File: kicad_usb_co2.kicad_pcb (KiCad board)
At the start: 2 copper layers, 90 x 54 mm, 10 parts, among them SW1 SW_Push, SW2 SW_Push, U1 MH-Z14A, U2 SeeeduinoXIAO

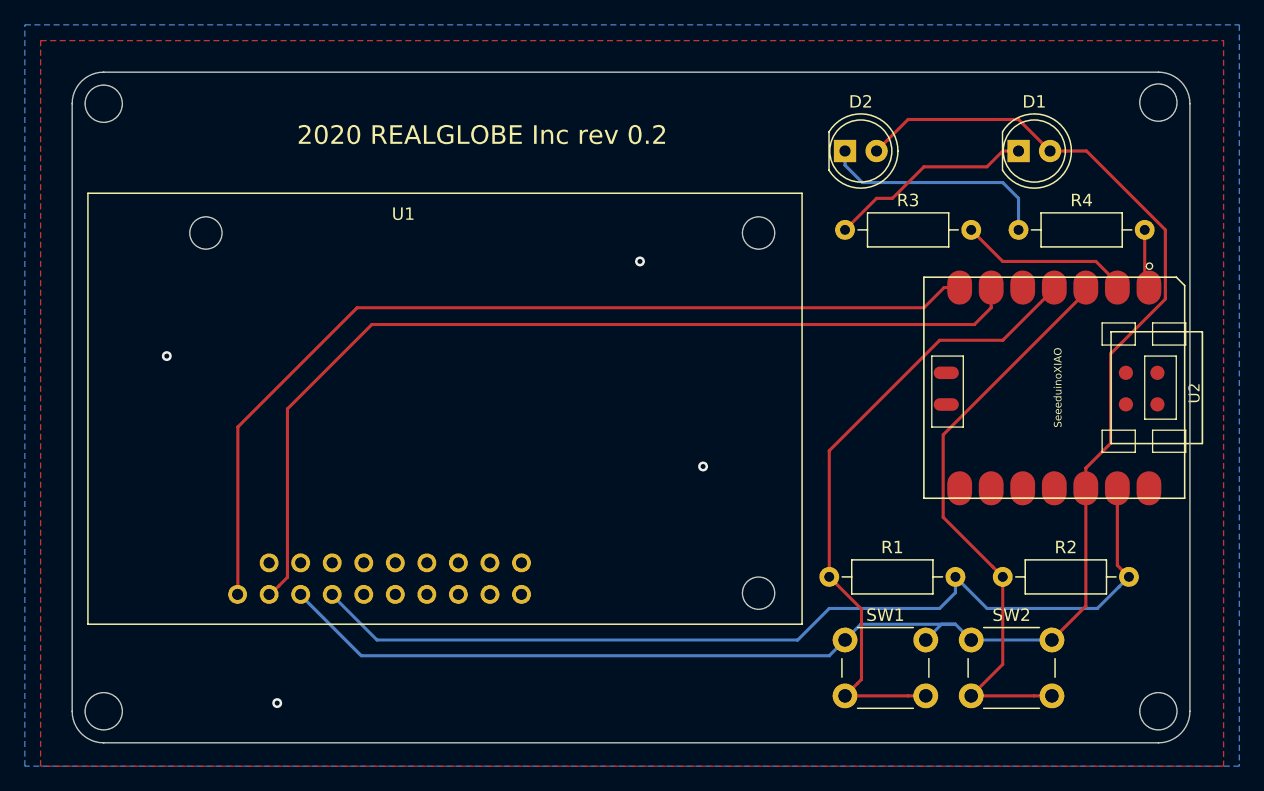
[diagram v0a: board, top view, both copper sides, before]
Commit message: LEDを削除、タクトスイッチからトグルスイッチに変更
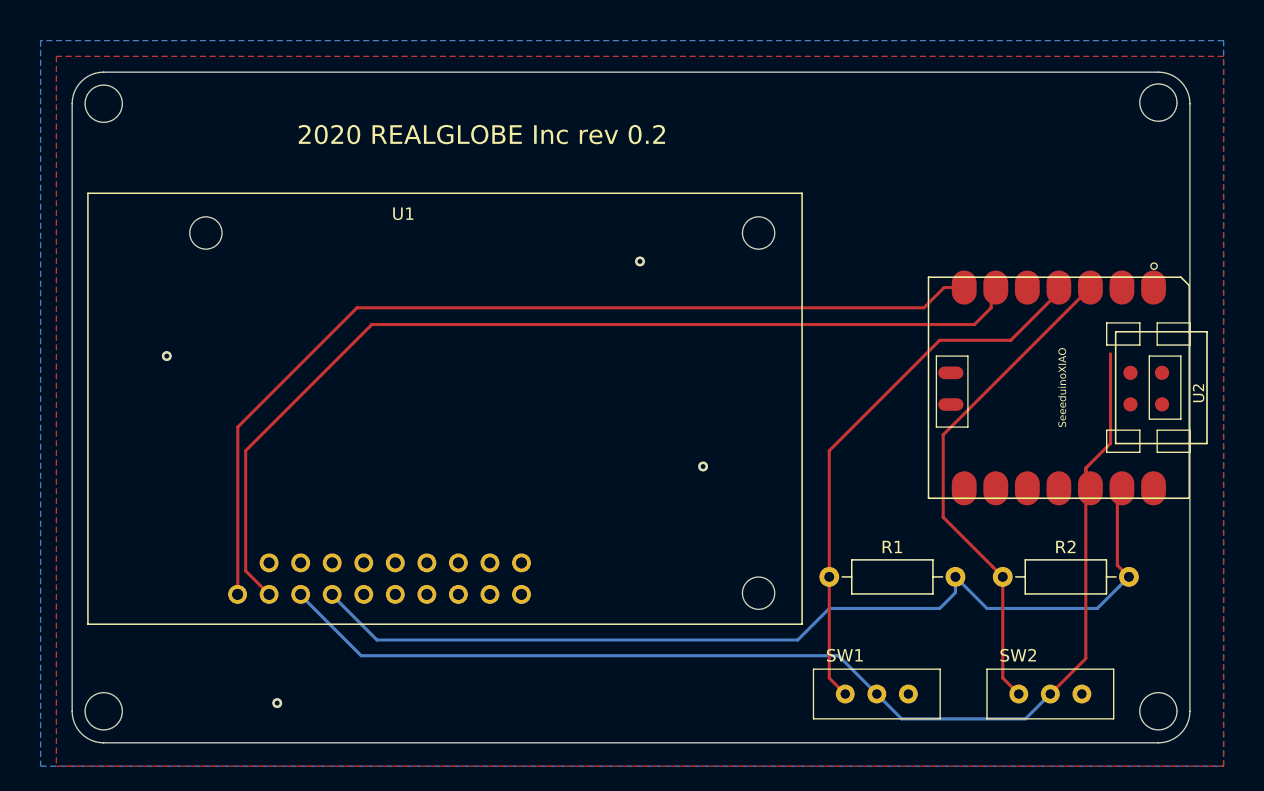
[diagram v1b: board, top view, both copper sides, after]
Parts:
- removed D1, D2: LED, LED_THT:LED_D5.0mm
- removed R3, R4: R, Resistor_THT:R_Axial_DIN0207_L6.3mm_D2.5mm_P10.16mm_Horizontal
- SW1, SW2: value SW_Push -> SW_SPDT; footprint Button_Switch_THT:SW_PUSH_6mm -> Mylib:SW_SLIDE_sengoku
- moved SW1 6.84 mm to (59.7, 52.1)
- moved SW2 6.48 mm to (73.7, 52.1)
- moved U2 0.37 mm to (69.0, 16.5)
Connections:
- SW1 pad 1: +3V3 -> Net-(R1-Pad1)
- SW1 pad 2: Net-(R1-Pad1) -> +3V3
- SW2 pad 1: +3V3 -> Net-(R2-Pad1)
- SW2 pad 2: Net-(R2-Pad1) -> +3V3
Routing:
- net +3V3: track 131.8 -> 96.3 mm
- net Net-(D2-Pad1): track 18.8 -> 0.00 mm
- net Net-(D1-Pad1): track 16.6 -> 0.00 mm
- net Net-(U2-Pad2): track 13.9 -> 0.00 mm
- net Net-(R2-Pad1): track 47.2 -> 40.0 mm
- net Net-(R1-Pad1): track 51.5 -> 44.4 mm
- net Net-(U2-Pad1): track 4.78 -> 0.00 mm
- net Net-(U1-Pad18): track 77.3 -> 78.8 mm
